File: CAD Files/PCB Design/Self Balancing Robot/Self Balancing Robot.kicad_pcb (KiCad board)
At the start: 2 copper layers, 82.5 x 53.5 mm, 17 parts, among them J1 Screw_Terminal_01x02, M1 Stepper_Motor_bipolar, M2 Stepper_Motor_bipolar, U2 TSR_1-2450

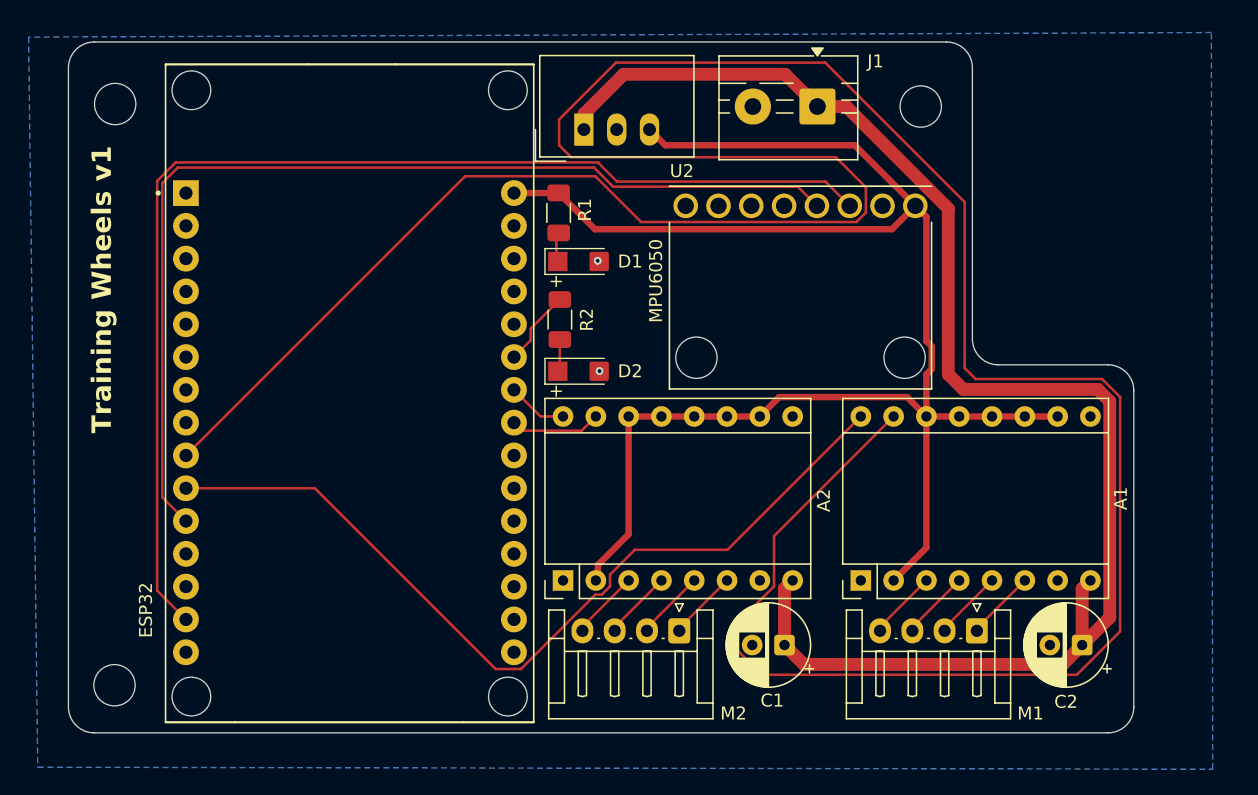
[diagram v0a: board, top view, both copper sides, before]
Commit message: v1.1: Added decoupling capacitors, XH60 connector. Entire layout redo Implemented traces on 2 layers + ground plane on bottom + ground pour on top.
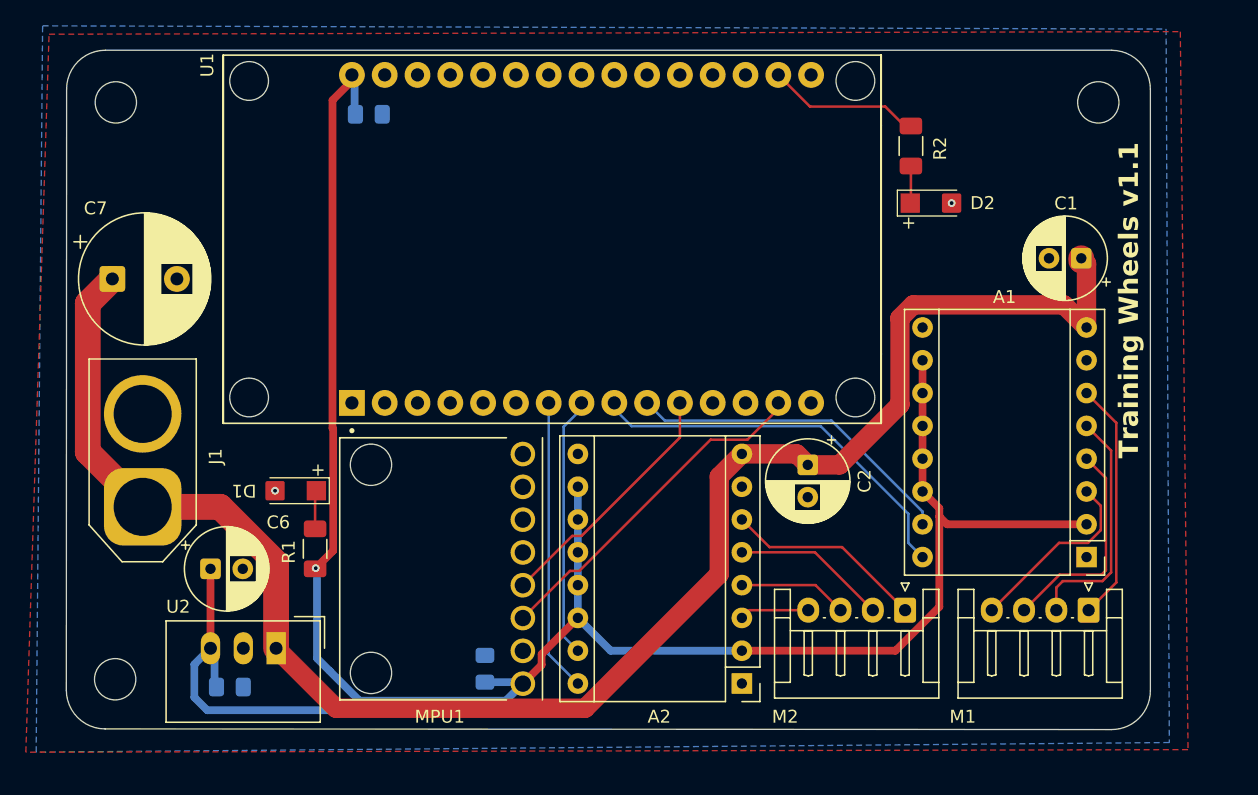
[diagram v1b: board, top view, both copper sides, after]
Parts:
- removed ESP32: DEVKIT_V1_ESP32-WROOM-32, TW Footprints:MODULE_DEVKIT_V1_ESP32-WROOM-32
- removed MPU6050: ~, TW Footprints:MODULE_GY-521
- added C3: 0.1 uF, Capacitor_SMD:C_0805_2012Metric_Pad1.18x1.45mm_HandSolder, B.Cu at (99.0, 90.0)
- added C4: 0.1 uF, Capacitor_SMD:C_0805_2012Metric_Pad1.18x1.45mm_HandSolder, B.Cu at (109.8, 45.6)
- added C5: 0.1 uF, Capacitor_SMD:C_0805_2012Metric_Pad1.18x1.45mm_HandSolder, B.Cu at (118.8, 88.5)
- added C6: 100 uF, TW Footprints:CP_Radial_D6.3mm_P2.50mm, F.Cu at (97.5, 80.8)
- added C7: 470 uF, Capacitor_THT:CP_Radial_D10.0mm_P5.00mm, F.Cu at (89.9, 58.4)
- added MPU1: GY-521, TW Footprints:MODULE_GY-521, F.Cu at (115.4, 80.8)
- added U1: DEVKIT_V1_ESP32-WROOM-32, TW Footprints:MODULE_DEVKIT_V1_ESP32-WROOM-32, F.Cu at (124.0, 55.2)
- C1, C2: value ECA1HM101 -> 100 uF
- J1: value Screw_Terminal_01x02 -> XT60 Female; footprint TerminalBlock:TerminalBlock_MaiXu_MX126-5.0-02P_1x02_P5.00mm -> Connector_AMASS:AMASS_XT60-F_1x02_P7.20mm_Vertical
- moved J1 60.8 mm to (92.2, 76.0), turned to 90 degrees
- moved U2 46.7 mm to (102.6, 87.0), turned to 180 degrees
- moved C1 37.8 mm to (164.9, 56.8)
- moved R1 32.1 mm to (105.6, 79.2), turned to 90 degrees
- moved R2 30.3 mm to (151.7, 48.1)
- moved D2 30.2 mm to (153.3, 52.5)
- moved D1 28.2 mm to (104.1, 74.8), turned to 180 degrees
- moved C2 25.4 mm to (143.8, 72.8), turned to -90 degrees
- moved A1 17.6 mm to (165.3, 79.9), turned to 180 degrees
- moved M2 17.6 mm to (151.3, 84.0)
- moved A2 16.0 mm to (138.6, 89.7), turned to 180 degrees
- moved REF** 13.8 mm to (166.2, 44.7)
- moved M1 8.80 mm to (165.5, 84.0)
- moved REF** 0.47 mm to (90.1, 89.3)
- moved REF** 0.14 mm to (90.2, 44.7)
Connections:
- R2 pad 1: /D27 -> /D16
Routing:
- net /Step1: track 229.0 -> 25.8 mm
- net /SCL: track 90.5 -> 26.5 mm
- net /SDA: track 79.3 -> 19.1 mm
- net VDD: track 135.0 -> 175.3 mm, vias 0 -> 1
- net /Direc1: track 66.7 -> 29.9 mm
- net /Direc2: track 4.65 -> 22.2 mm
- net +12V: track 115.8 -> 132.6 mm
- net /L_2B: track 5.44 -> 18.7 mm
- net /L_2A: track 5.42 -> 18.6 mm
- net /Step2: track 7.05 -> 19.8 mm
- net /D16: track 0.00 -> 11.9 mm
- net /L_1A: track 5.40 -> 16.9 mm
- net /R_2B: track 5.43 -> 15.5 mm
- net /L_1B: track 5.39 -> 14.5 mm
- net /R_2A: track 5.42 -> 12.0 mm
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- added copper zone on F.Cu, net GND
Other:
- board size 82.5 x 53.5 mm -> 83.9 x 52.6 mm
- board text added: "Training Wheels v1.1"
- board text removed: "Training Wheels v1"

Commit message: Assigned ESP-32 and 1206 LED 3dmodels to footprints
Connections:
- net /D16 renamed /D36
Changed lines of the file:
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@@
 	(net 43 "unconnected-(U1-D25-Pad23)")
 	(net 44 "unconnected-(U1-D14-Pad26)")
-	(net 45 "/D16")
+	(net 45 "/D36")
 	(net 46 "unconnected-(U1-RX2-Pad6)")
 	(footprint "Resistor_SMD:R_1206_3216Metric_Pad1.30x1.75mm_HandSolder"
@@
 			(layers "F.Cu" "F.Mask" "F.Paste")
 			(roundrect_rratio 0.192308)
-			(net 45 "/D16")
+			(net 45 "/D36")
 			(pintype "passive")
 		)
@@
 			(layers "*.Cu" "*.Mask")
 			(remove_unused_layers no)
-			(net 45 "/D16")
+			(net 45 "/D36")
 			(pinfunction "VP")
 			(pintype "bidirectional")
@@
 		)
 		(embedded_fonts no)
+		(model "C:/Users/parad/OneDrive/Documents/Training Wheels/CAD Files/PCB Design/Kicad Tools/esp32_30pin-v3.step"
+			(offset
+				(xyz 12 23 12)
+			)
+			(scale
+				(xyz 1 1 1)
+			)
+			(rotate
+				(xyz -0 -0 -180)
+			)
+		)
+		(model "${KICAD9_3DMODEL_DIR}/Connector_PinSocket_2.54mm.3dshapes/PinSocket_1x15_P2.54mm_Vertical.step"
+			(offset
+				(xyz -13 15.5 0)
+			)
+			(scale
+				(xyz 1 1 1)
+			)
+			(rotate
+				(xyz -0 -0 -0)
+			)
+		)
+		(model "${KICAD9_3DMODEL_DIR}/Connector_PinSocket_2.54mm.3dshapes/PinSocket_1x15_P2.54mm_Vertical.step"
+			(offset
+				(xyz 13 15.5 0)
+			)
+			(scale
+				(xyz 1 1 1)
+			)
+			(rotate
+				(xyz -0 -0 -0)
+			)
+		)
+		(model "${KICAD9_3DMODEL_DIR}/Connector_PinHeader_2.54mm.3dshapes/PinHeader_1x15_P2.54mm_Vertical.step"
+			(offset
+				(xyz 13 -20 11)
+			)
+			(scale
+				(xyz 1 1 1)
+			)
+			(rotate
+				(xyz -180 -0 -0)
+			)
+		)
+		(model "${KICAD9_3DMODEL_DIR}/Connector_PinHeader_2.54mm.3dshapes/PinHeader_1x15_P2.54mm_Vertical.step"
+			(offset
+				(xyz -13 -20 11)
+			)
+			(scale
+				(xyz 1 1 1)
+			)
+			(rotate
+				(xyz -180 -0 -0)
+			)
+		)
 	)
 	(footprint "MountingHole:MountingHole_3.2mm_M3"
@@
 		)
 		(embedded_fonts no)
+		(model "${KICAD9_3DMODEL_DIR}/LED_SMD.3dshapes/LED_1206_3216Metric.step"
+			(offset
+				(xyz 0 0 0)
+			)
+			(scale
+				(xyz 1 1 1)
+			)
+			(rotate
+				(xyz 0 0 0)
+			)
+		)
 	)
 	(footprint "TW Footprints:CP_Radial_D6.3mm_P2.50mm"
@@
 		)
 		(embedded_fonts no)
+		(model "${KICAD9_3DMODEL_DIR}/LED_SMD.3dshapes/LED_1206_3216Metric.step"
+			(offset
+				(xyz 0 0 0)
+			)
+			(scale
+				(xyz 1 1 1)
+			)
+			(rotate
+				(xyz 0 0 0)
+			)
+		)
 	)
 	(footprint "MountingHole:MountingHole_3.2mm_M3"

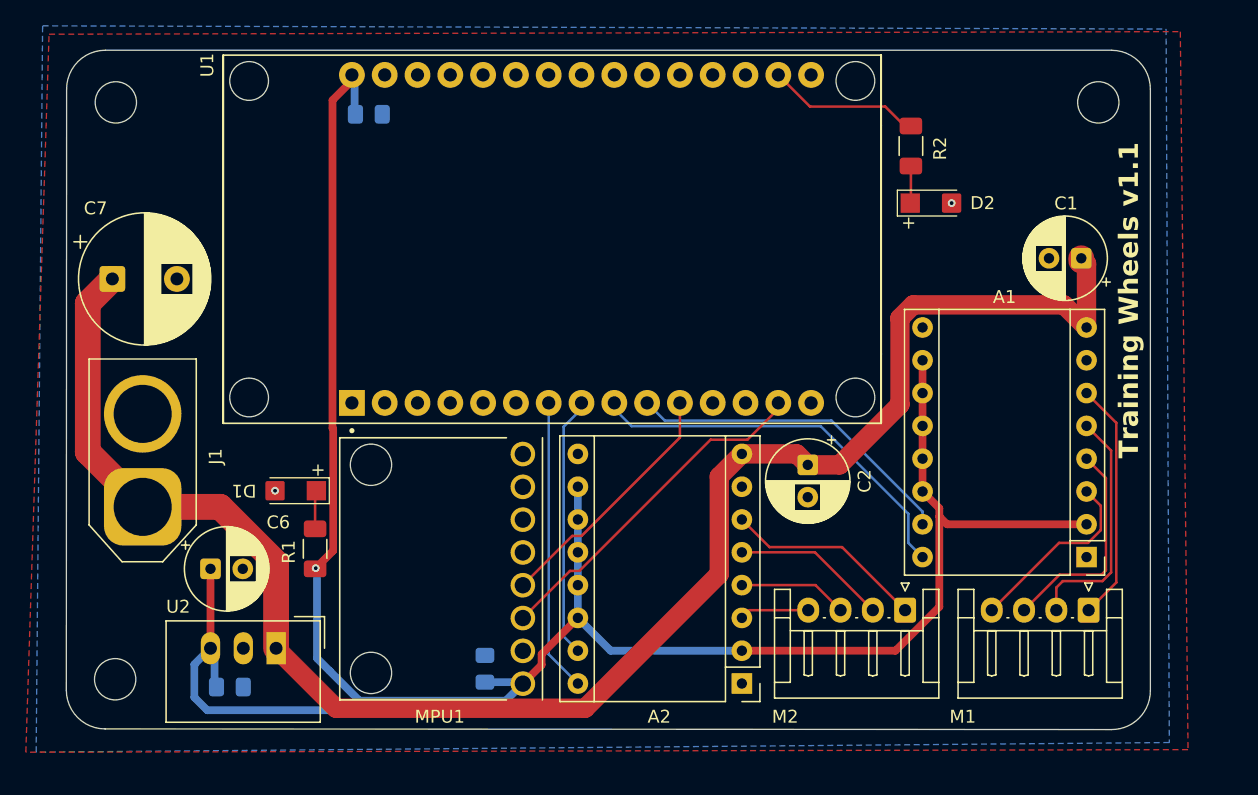
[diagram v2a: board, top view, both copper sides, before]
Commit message: v1.2: Modified layout to accommodate wider traces. 2.0 mm for 12V and 1.5mm for the motor lines. Rotated MPU to have 12V line farther away
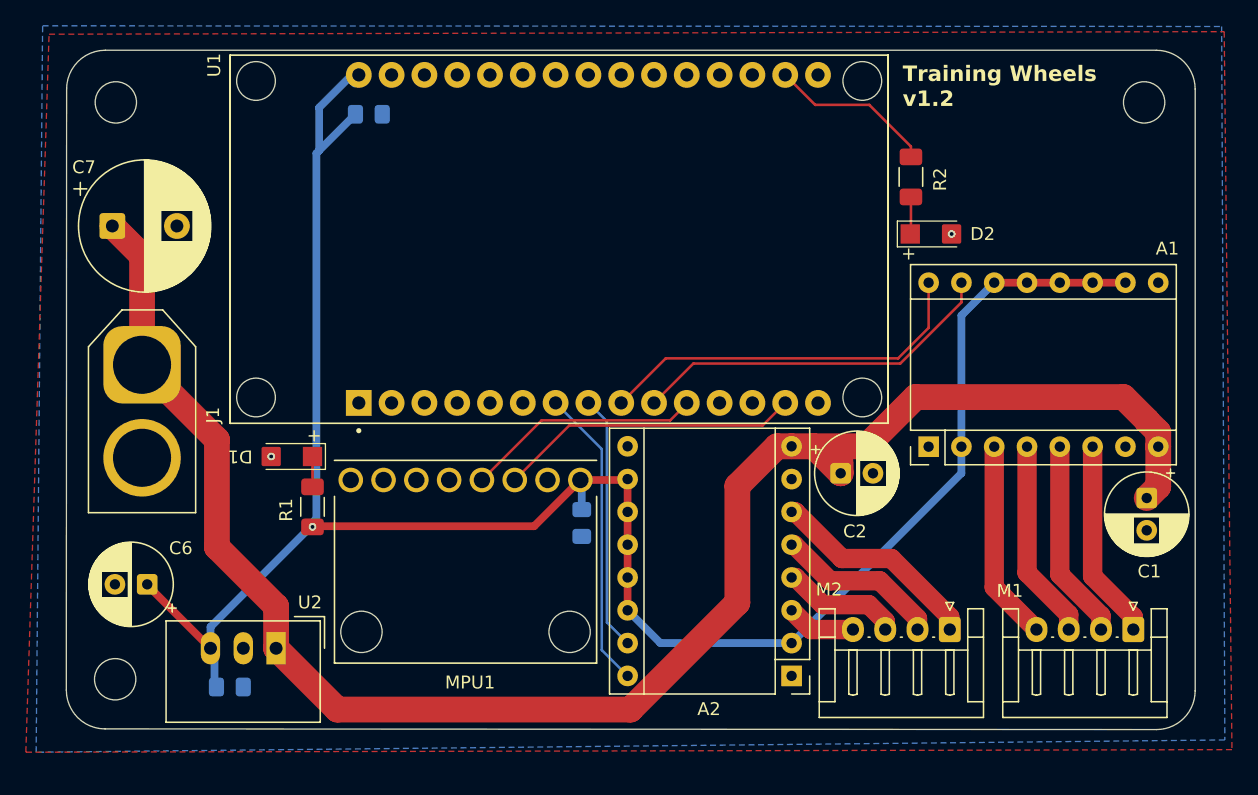
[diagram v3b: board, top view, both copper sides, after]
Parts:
- moved C1 19.2 mm to (170.0, 75.3), turned to -90 degrees
- moved A1 14.9 mm to (153.1, 71.3), turned to 90 degrees
- moved C5 13.6 mm to (126.2, 77.2), turned to -90 degrees
- moved J1 11.0 mm to (92.2, 65.0), turned to -90 degrees
- moved C6 5.04 mm to (92.6, 82.0), turned to 180 degrees
- moved C7 4.10 mm to (89.9, 54.2)
- moved A2 3.90 mm to (142.5, 89.1)
- moved M1 3.77 mm to (169.0, 85.5)
- moved M2 3.77 mm to (154.8, 85.5)
- moved REF** 3.55 mm to (169.8, 44.7)
- moved R1 3.26 mm to (105.4, 76.0)
- moved D1 2.67 mm to (103.8, 72.1)
- moved C2 2.63 mm to (146.3, 73.4), turned to 0 degrees
- moved D2 2.39 mm to (153.3, 54.9)
- moved R2 2.39 mm to (151.7, 50.5)
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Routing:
- net VDD: track 175.3 -> 160.8 mm
- net /L_2B: track 18.7 -> 15.5 mm
- net /L_2A: track 18.6 -> 15.5 mm
- net /Step1: track 25.8 -> 28.9 mm
- net /SCL: track 26.5 -> 23.4 mm
- net /D36: track 11.9 -> 13.3 mm
- net /L_1A: track 16.9 -> 15.5 mm
- net +12V: track 132.6 -> 133.9 mm
- net /Direc2: track 22.2 -> 23.4 mm
- net /L_1B: track 14.5 -> 15.5 mm
- net /R_2B: track 15.5 -> 16.6 mm
- net /R_2A: track 12.0 -> 13.0 mm
- net /R_1A: track 8.44 -> 9.30 mm
- net /SDA: track 19.1 -> 18.4 mm
- net Net-(D1-K): track 2.99 -> 2.39 mm
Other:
- board size 83.9 x 52.6 mm -> 87.4 x 52.6 mm
- board text added: "Training Wheels v1.2"
- board text removed: "Training Wheels v1.1"

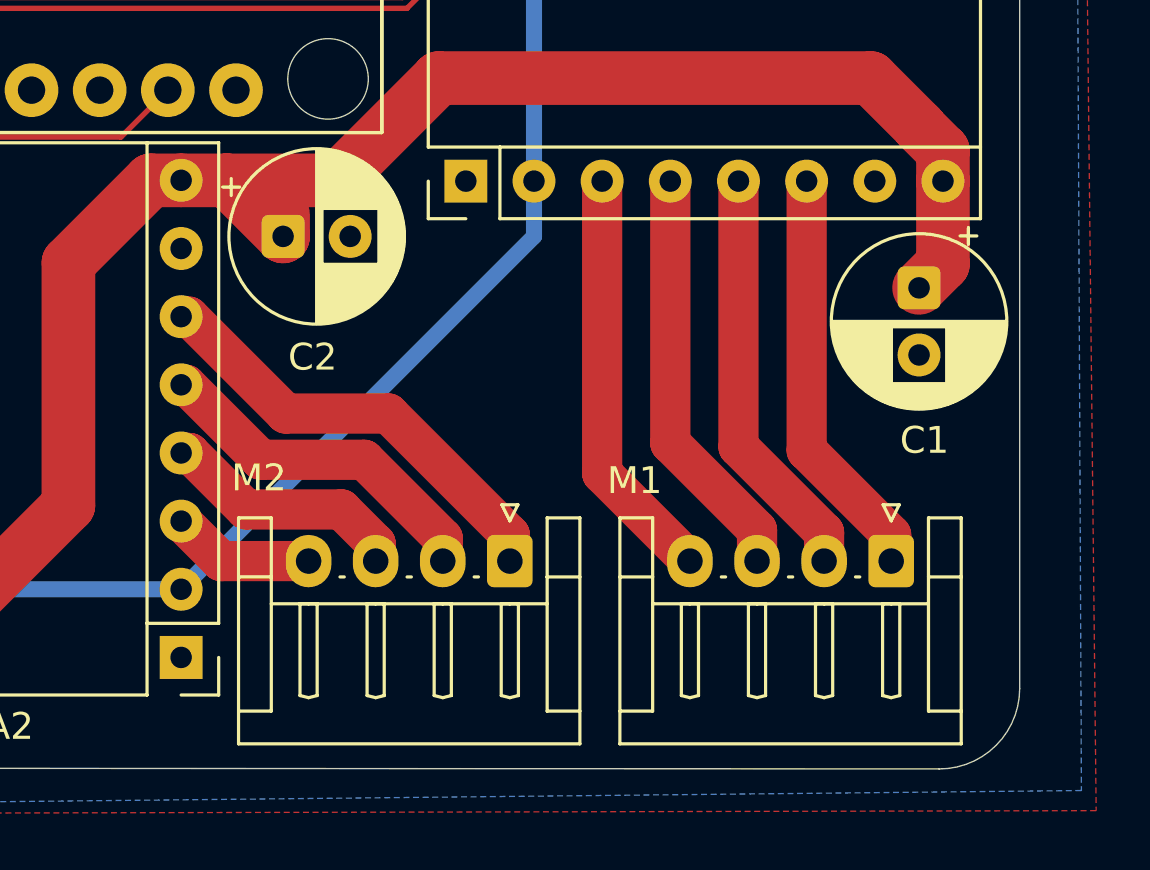
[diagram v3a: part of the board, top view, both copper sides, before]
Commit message: replace servo connectors from JST- EH to JST-XH because more common connector type
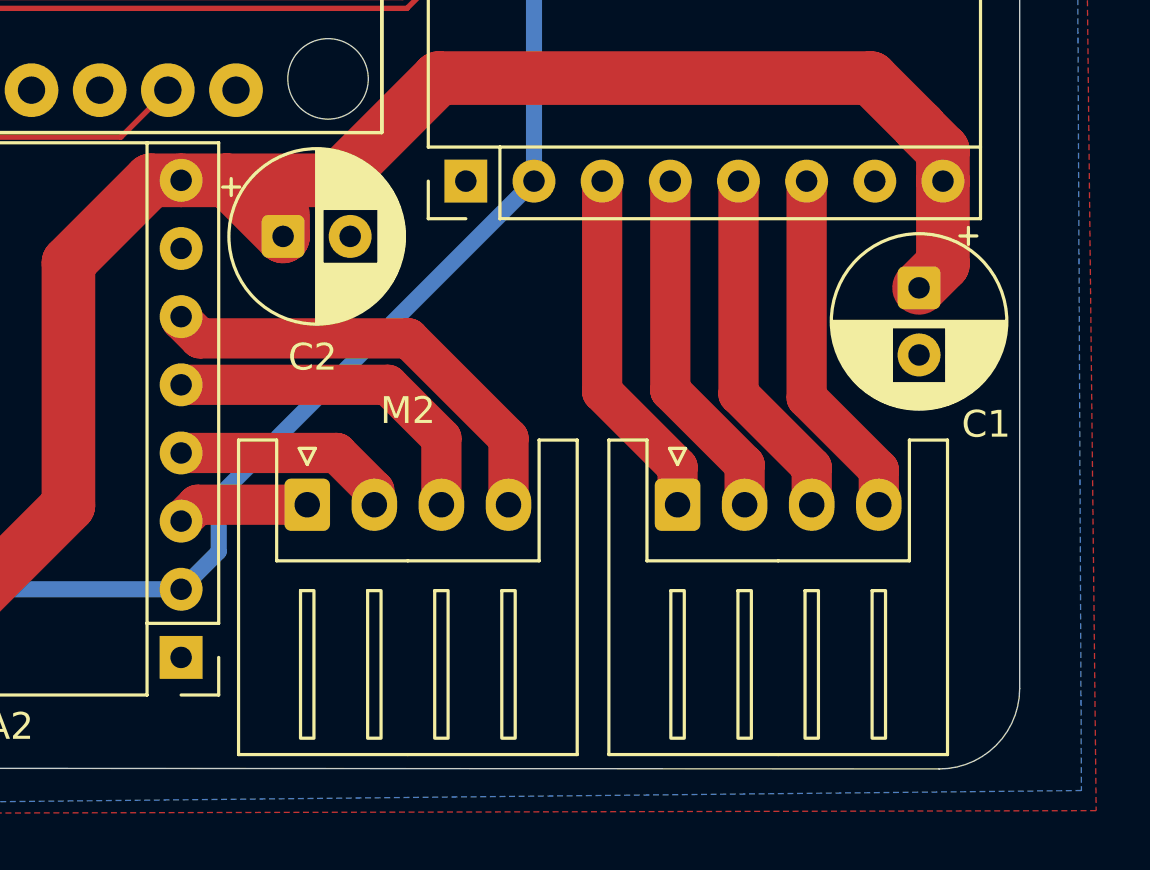
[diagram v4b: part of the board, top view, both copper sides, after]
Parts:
- M1, M2: footprint Connector_JST:JST_EH_S4B-EH_1x04_P2.50mm_Horizontal -> Connector_JST:JST_XH_S4B-XH-A_1x04_P2.50mm_Horizontal
- moved M1 8.23 mm to (161.0, 83.4), turned to 0 degrees
- moved M2 7.84 mm to (147.2, 83.4), turned to 0 degrees
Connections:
- M1 pad 1: /L_2B -> /L_1B
- M1 pad 2: /L_2A -> /L_1A
- M1 pad 3: /L_1A -> /L_2A
- M1 pad 4: /L_1B -> /L_2B
- M2 pad 1: /R_2B -> /R_1B
- M2 pad 2: /R_2A -> /R_1A
- M2 pad 3: /R_1A -> /R_2A
- M2 pad 4: /R_1B -> /R_2B
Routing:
- net /L_2A: track 15.5 -> 13.2 mm
- net /L_1B: track 15.5 -> 13.2 mm
- net /L_1A: track 15.5 -> 13.2 mm
- net /L_2B: track 15.5 -> 13.2 mm
- net /R_1A: track 9.30 -> 8.31 mm
